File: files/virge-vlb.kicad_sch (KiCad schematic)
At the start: 1 part, among them U1 86C375_layout

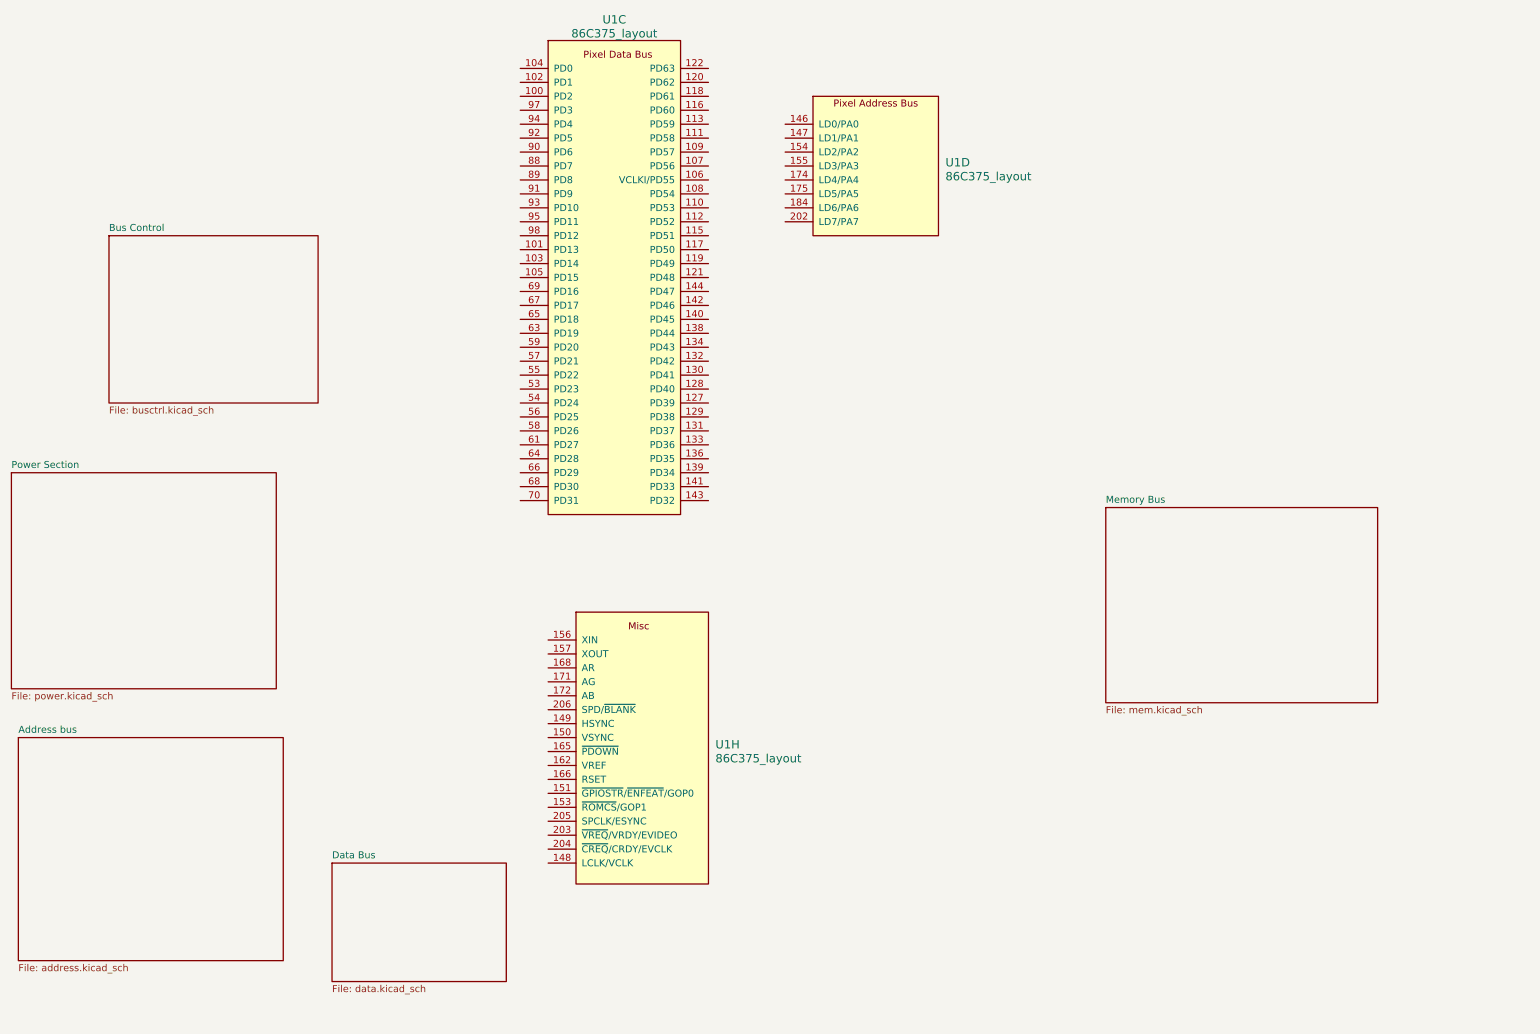
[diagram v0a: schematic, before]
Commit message: work on the memory bus, fixed symbols
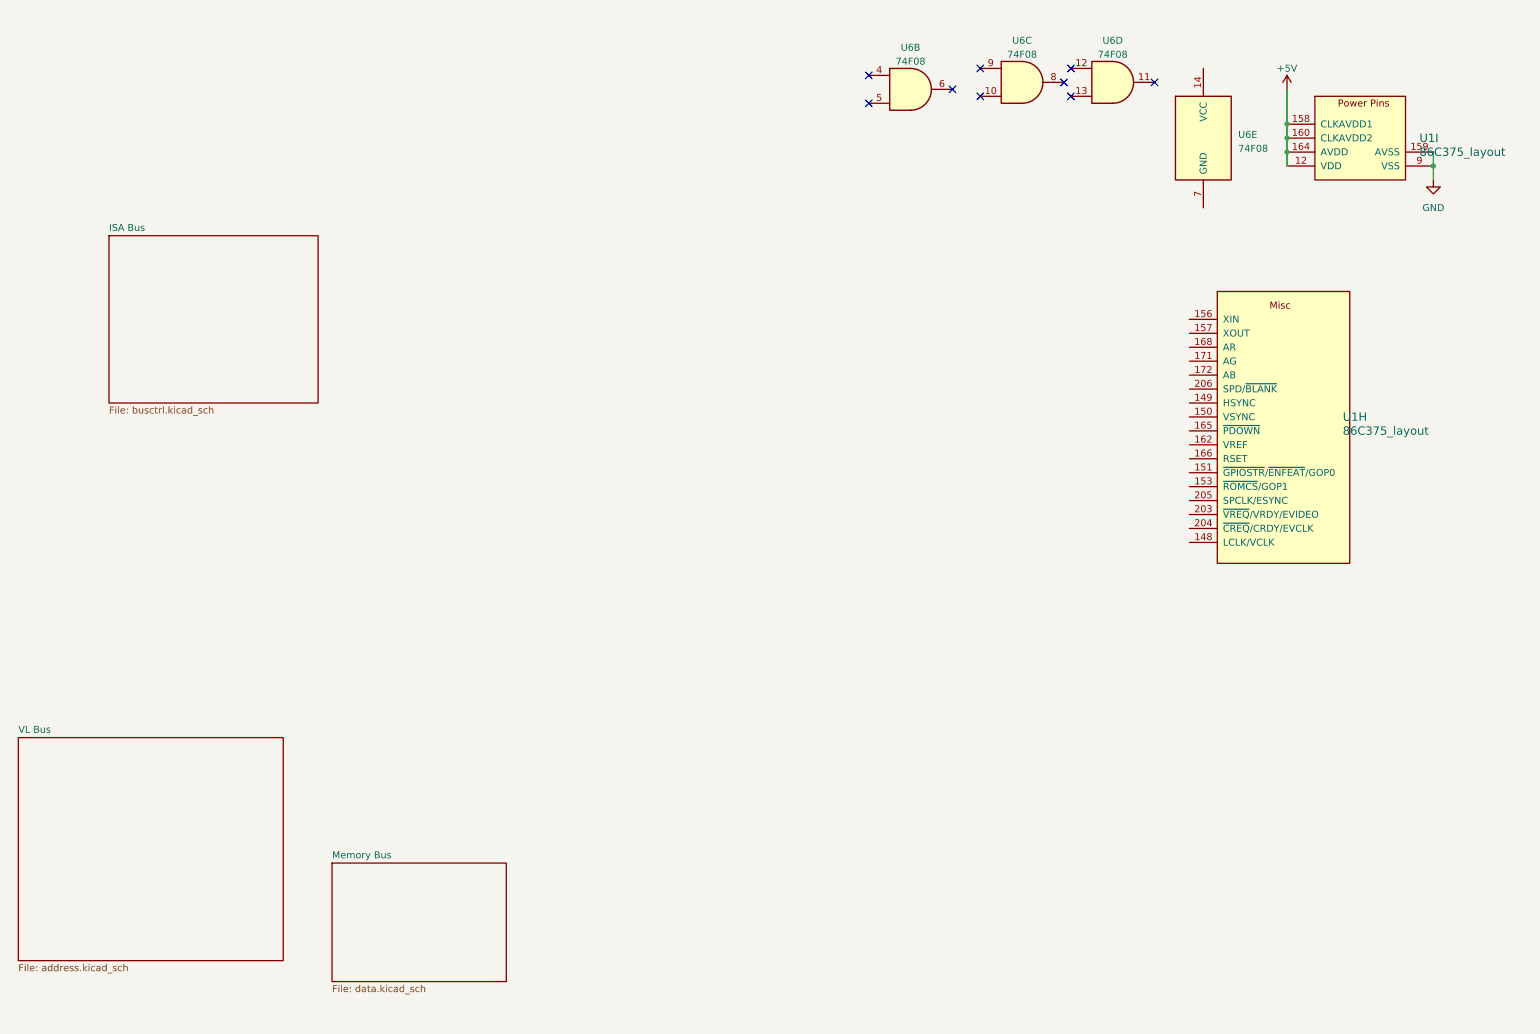
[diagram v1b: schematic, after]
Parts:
- removed unit 3 of U1
- removed unit 4 of U1
- added unit 9 of U1
- added U6: 74F08, Package_SO:SOIC-14_3.9x8.7mm_P1.27mm, symbol 74xx:74LS08
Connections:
- new net +5V: U1.12 (VDD), U1.137 (VDD), U1.158 (CLKAVDD1), U1.160 (CLKAVDD2), U1.164 (AVDD), U1.169 (AVDD), U1.170 (AVDD), U1.192 (VDD), U1.37 (VDD), U1.62 (VDD), U1.81 (VDD), U1.96 (VDD)
- new net GND: U1.114 (VSS), U1.123 (VSS), U1.126 (VSS), U1.135 (VSS), U1.145 (VSS), U1.159 (AVSS), U1.161 (AVSS), U1.163 (AVSS), U1.167 (AVSS), U1.173 (AVSS), U1.195 (VSS), U1.22 (VSS), U1.32 (VSS), U1.47 (VSS), U1.60 (VSS), U1.71 (VSS), U1.87 (VSS), U1.9 (VSS), U1.99 (VSS)
- no-connect marks 0 -> 9
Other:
- sheet Address bus renamed VL Bus
- sheet Bus Control renamed ISA Bus
- removed sheet Data Bus
- removed sheet Power Section
- sheet Memory Bus: file mem.kicad_sch -> data.kicad_sch
- moved on the sheet: U1H

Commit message: changed memory chips, more progress
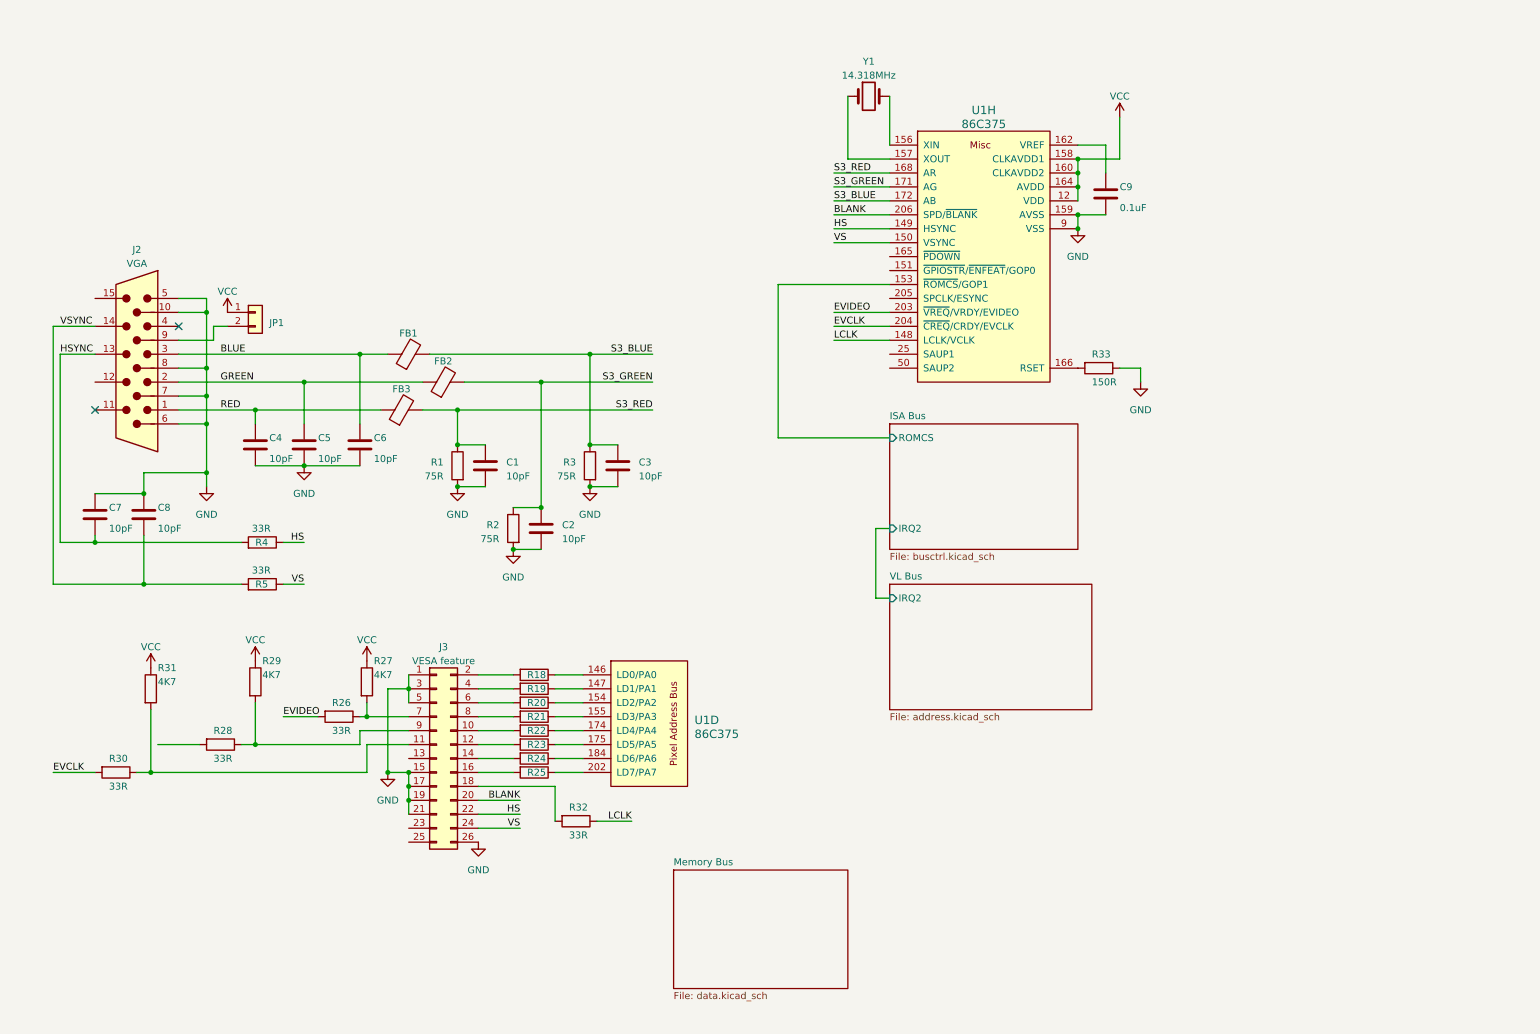
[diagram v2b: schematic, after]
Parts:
- removed U1: 86C375_layout, Package_QFP:PQFP-208_28x28mm_P0.5mm, symbol virge:86C375_layout
- removed U6: 74F08, Package_SO:SOIC-14_3.9x8.7mm_P1.27mm, symbol 74xx:74LS08
- added C1, C2, C3, C4, C5, C6, C7, C8: 10pF, Capacitor_SMD:C_0805_2012Metric_Pad1.18x1.45mm_HandSolder, symbol Device:C
- added C9: 0.1uF, Capacitor_SMD:C_0805_2012Metric_Pad1.18x1.45mm_HandSolder, symbol Device:C
- added FB1, FB2, FB3: FerriteBead, symbol Device:FerriteBead
- added J2: VGA, Connector_Dsub:DSUB-15-HD_Female_Horizontal_P2.29x1.98mm_EdgePinOffset8.35mm_Housed_MountingHolesOffset10.89mm, symbol Connector:DE15_Plug_HighDensity
- added J3: VESA feature, symbol Connector_Generic:Conn_02x13_Odd_Even
- added JP1: Conn_01x02, Connector_PinHeader_2.54mm:PinHeader_1x02_P2.54mm_Vertical, symbol Connector_Generic:Conn_01x02
- added R1, R2, R3: 75R, Resistor_SMD:R_0805_2012Metric_Pad1.20x1.40mm_HandSolder, symbol Device:R
- added R18, R19, R20, R21, R22, R23, R24, R25, R26, R28, R30, R32, R4, R5: 33R, Resistor_SMD:R_0805_2012Metric_Pad1.20x1.40mm_HandSolder, symbol Device:R
- added R27, R29, R31: 4K7, Resistor_SMD:R_0805_2012Metric_Pad1.20x1.40mm_HandSolder, symbol Device:R
- added R33: 150R, Resistor_SMD:R_0805_2012Metric_Pad1.20x1.40mm_HandSolder, symbol Device:R
- added U1: 86C375, Package_QFP:PQFP-208_28x28mm_P0.5mm, symbol virge:86C375
- added Y1: 14.318MHz, Crystal:Crystal_HC18-U_Vertical, symbol Device:Crystal
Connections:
- net GND: now also C1.2, C2.2, C3.2, C4.2, C5.2, C6.2, C7.1, C8.1, C9.2, J2.10, J2.5, J2.6, J2.7, J2.8, J3.1 (Pin_1), J3.15 (Pin_15), J3.17 (Pin_17), J3.19 (Pin_19), J3.21 (Pin_21), J3.26 (Pin_26), J3.3 (Pin_3), J3.5 (Pin_5), R1.2, R2.2, R3.2, R33.1, U1.114 (VSS), U1.123 (VSS), U1.126 (VSS), U1.135 (VSS), U1.145 (VSS), U1.159 (AVSS), U1.161 (AVSS), U1.163 (AVSS), U1.167 (AVSS), U1.173 (AVSS), U1.195 (VSS), U1.22 (VSS), U1.32 (VSS), U1.47 (VSS), U1.60 (VSS), U1.71 (VSS), U1.87 (VSS), U1.9 (VSS), U1.99 (VSS)
- new net: J3.11 (Pin_11), R30.1, R31.2
- new net: R18.1, U1.146 (LD0/PA0)
- new net: R19.1, U1.147 (LD1/PA1)
- new net: R20.1, U1.154 (LD2/PA2)
- new net: R21.1, U1.155 (LD3/PA3)
- new net: R22.1, U1.174 (LD4/PA4)
- new net: R23.1, U1.175 (LD5/PA5)
- new net: R24.1, U1.184 (LD6/PA6)
- new net: R25.1, U1.202 (LD7/PA7)
- new net: J3.14 (Pin_14), R24.2
- new net: J3.10 (Pin_10), R22.2
- new net: J3.12 (Pin_12), R23.2
- new net: J3.16 (Pin_16), R25.2
- new net: J3.18 (Pin_18), R32.2
- new net: J3.2 (Pin_2), R18.2
- new net: J3.4 (Pin_4), R19.2
- new net: J3.6 (Pin_6), R20.2
- new net: J3.7 (Pin_7), R26.1, R27.2
- new net: J3.8 (Pin_8), R21.2
- new net: J3.9 (Pin_9), R28.1, R29.2
- new net: J2.9, JP1.2 (Pin_2)
- new net: U1.156 (XIN), Y1.2
- new net: U1.157 (XOUT), Y1.1
- new net: C9.1, U1.162 (VREF)
- new net: R33.2, U1.166 (RSET)
- new net BLANK: J3.20 (Pin_20), U1.206 (SPD/~{BLANK})
- new net BLUE: C6.1, FB1.1, J2.3
- new net EVCLK: R30.2, U1.204 (~{CREQ}/CRDY/EVCLK)
- new net EVIDEO: R26.2, U1.203 (~{VREQ}/VRDY/EVIDEO)
- new net GREEN: C5.1, FB2.1, J2.2
- new net HS: J3.22 (Pin_22), R4.1, U1.149 (HSYNC)
- new net HSYNC: C7.2, J2.13, R4.2
- new net ISA Bus/ROMCS: U1.153 (~{ROMCS}/GOP1)
- new net LCLK: R32.1, U1.148 (LCLK/VCLK)
- new net RED: C4.1, FB3.1, J2.1
- new net S3_BLUE: C3.1, FB1.2, R3.1, U1.172 (AB)
- new net S3_GREEN: C2.1, FB2.2, R2.1, U1.171 (AG)
- new net S3_RED: C1.1, FB3.2, R1.1, U1.168 (AR)
- new net VCC: JP1.1 (Pin_1), R27.1, R29.1, R31.1, U1.12 (VDD), U1.137 (VDD), U1.158 (CLKAVDD1), U1.160 (CLKAVDD2), U1.164 (AVDD), U1.169 (AVDD), U1.170 (AVDD), U1.192 (VDD), U1.37 (VDD), U1.62 (VDD), U1.81 (VDD), U1.96 (VDD)
- new net VS: J3.24 (Pin_24), R5.1, U1.150 (VSYNC)
- new net VSYNC: C8.2, J2.14, R5.2
- no-connect marks 9 -> 2
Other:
- sheet ISA Bus ports: added IRQ2, ROMCS; removed none
- sheet VL Bus ports: added IRQ2; removed none
